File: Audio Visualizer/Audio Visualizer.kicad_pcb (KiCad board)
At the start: 2 copper layers, 103.5 x 30.2 mm, 120 parts, among them J1 Screw_Terminal_01x04, J2 Screw_Terminal_01x04, J3 Screw_Terminal_01x02, Q10 MMBT3904, Q11 MMBT3904, Q12 MMBT3904, Q13 MMBT3904, Q14 MMBT3904, Q15 MMBT3904, Q16 MMBT3904, Q17 MMBT3904, Q18 MMBT3904, Q19 MMBT3904, Q2 MMBT3904, Q20 MMBT3904, Q21 MMBT3904, Q3 MMBT3904, Q4 MMBT3904, Q5 MMBT3904, Q6 MMBT3904, Q7 MMBT3904, Q8 MMBT3904, Q9 MMBT3904, U1 LM358

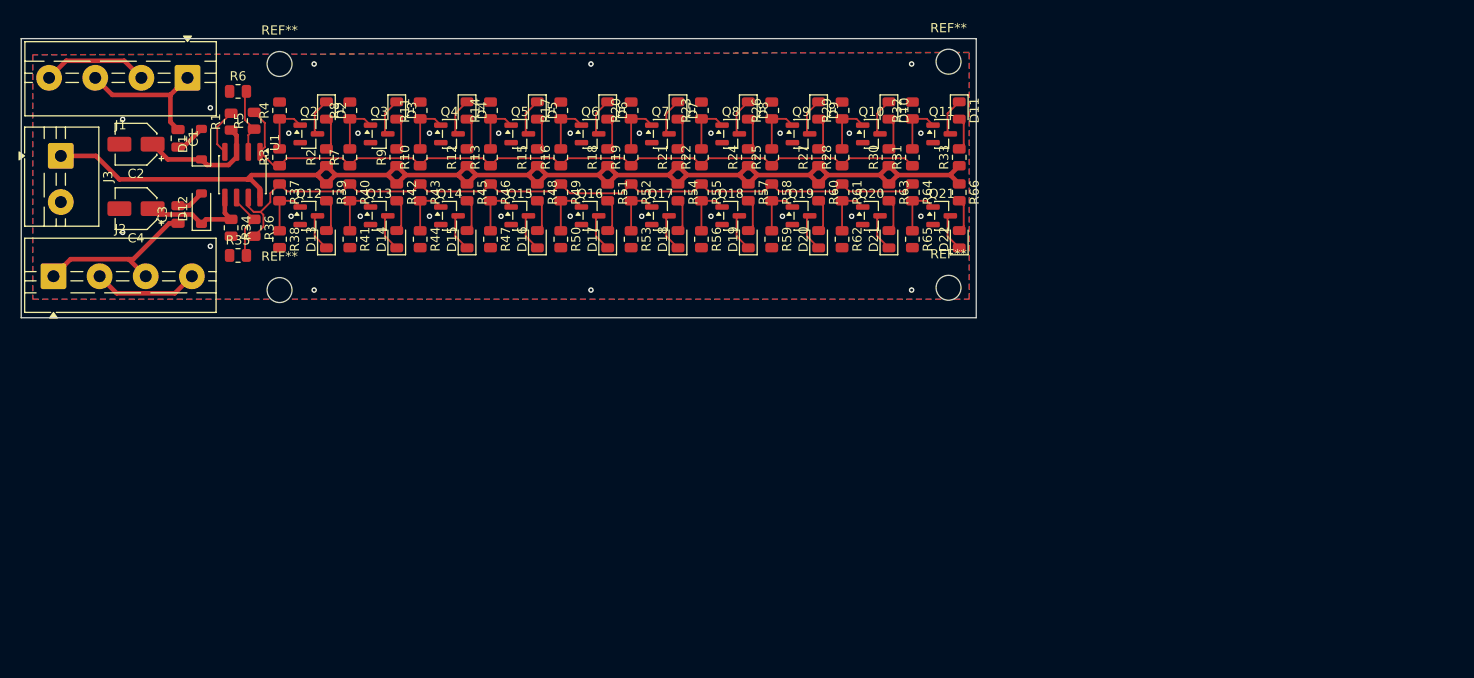
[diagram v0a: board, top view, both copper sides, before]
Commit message: Audio Visualizer: move terminal blocks and electrolytics to back side
Front face now flush for the LED ladder. THT terminals flipped with pads
kept on the same holes/nets; SMD electrolytics reconnected to front
traces with a via per pad; GND zones refilled. DRC: 0 errors,
0 unconnected. Adds back-side render.

Co-Authored-By: Claude Fable 5 <noreply@anthropic.com>
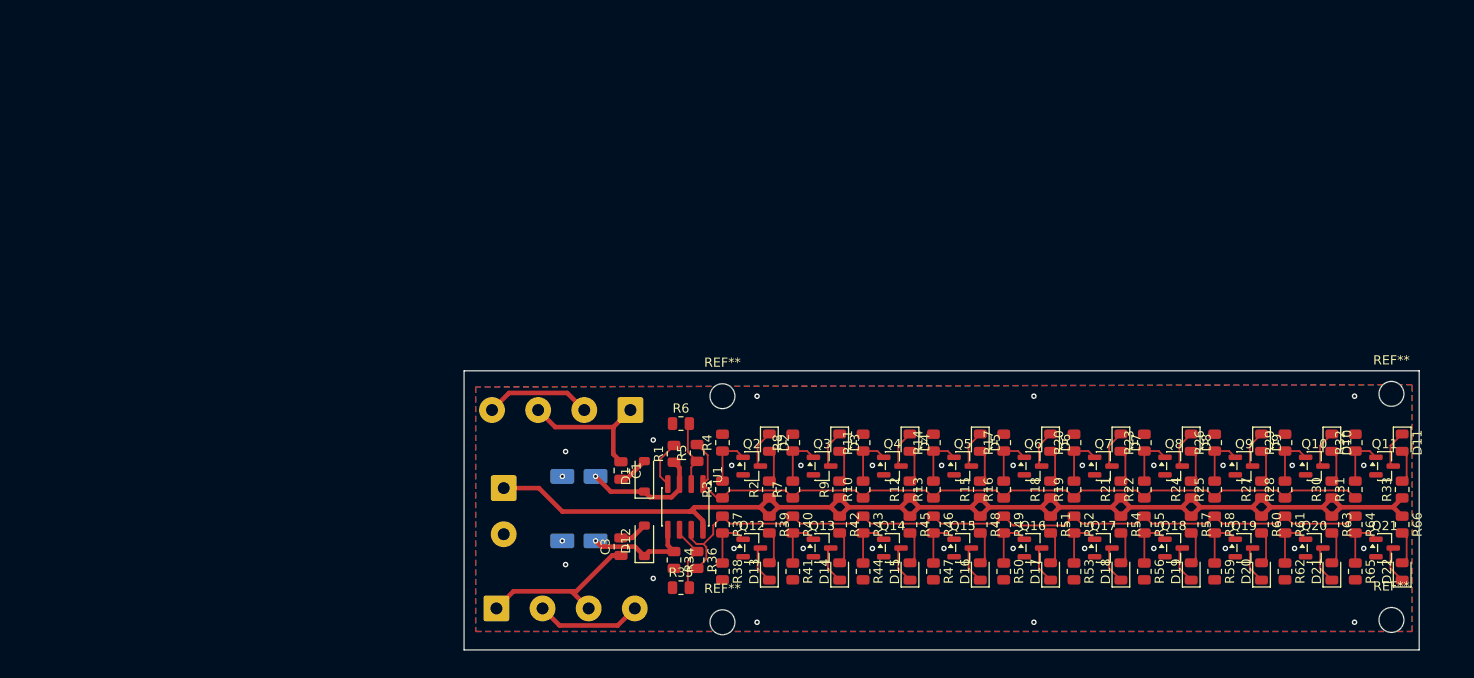
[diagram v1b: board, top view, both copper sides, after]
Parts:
- C2, C4, J1, J2, J3: moved to B.Cu
- moved C1 60.0 mm to (103.2, 95.1)
- moved C3 60.0 mm to (103.2, 103.3)
- moved D19 60.0 mm to (165.1, 106.0)
- moved D8 60.0 mm to (165.1, 92.0)
- moved J1 60.0 mm to (104.3, 88.5)
- moved Q18 60.0 mm to (163.1, 103.5)
- moved Q8 60.0 mm to (163.1, 94.6)
- moved R10 60.0 mm to (129.5, 97.1)
- moved R11 60.0 mm to (129.5, 92.0)
- moved R13 60.0 mm to (137.1, 97.1)
- moved R14 60.0 mm to (137.1, 92.0)
- moved R24 60.0 mm to (165.1, 97.1)
- moved R28 60.0 mm to (175.2, 97.1)
- moved R29 60.0 mm to (175.2, 92.0)
- moved R43 60.0 mm to (129.5, 100.9)
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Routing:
- net Net-(D1-K): vias 0 -> 1
- net Net-(D12-K): vias 0 -> 1
- net GND: vias 30 -> 32

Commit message: Audio Visualizer: face terminal block openings outward
Rotated J1/J2/J3 180deg about their pad rows (pin order reverses on the
holes) and swapped the matching net labels in the schematic (IN_L+/-,
IN_R+/-, +12V/GND) so every hole keeps its original net. Zones
refilled. DRC: 0 errors, 0 unconnected, 0 parity. All renders redone.

Co-Authored-By: Claude Fable 5 <noreply@anthropic.com>
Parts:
- moved J1 15.0 mm to (89.3, 88.5), turned to 0 degrees
- moved J2 15.0 mm to (104.8, 110.0), turned to 180 degrees
- moved J3 5.00 mm to (90.5, 102.0), turned to 90 degrees
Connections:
- J1 pad 1: /IN_R+ -> /IN_R-
- J1 pad 2: /IN_R- -> /IN_R+
- J1 pad 3: /IN_R+ -> /IN_R-
- J1 pad 4: /IN_R- -> /IN_R+
- J2 pad 1: /IN_L+ -> /IN_L-
- J2 pad 2: /IN_L- -> /IN_L+
- J2 pad 3: /IN_L+ -> /IN_L-
- J2 pad 4: /IN_L- -> /IN_L+
- J3 pad 1: /+12V -> GND
- J3 pad 2: GND -> /+12V

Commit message: Audio Visualizer: encode VU ladder LED colors (5 green, 4 orange, 1 red per row)
Co-Authored-By: Claude Fable 5 <noreply@anthropic.com>
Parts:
- D10, D18, D19, D20, D21, D7, D8, D9: value LED -> LED-ORANGE
- D11, D22: value LED -> LED-RED
- D13, D14, D15, D16, D17, D2, D3, D4, D5, D6: value LED -> LED-GREEN
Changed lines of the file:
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@@
 			)
 		)
-		(property "Value" "LED"
+		(property "Value" "LED-ORANGE"
 			(at 0 1.65 270)
 			(layer "F.Fab")
@@
 			)
 		)
-		(property "Value" "LED"
+		(property "Value" "LED-ORANGE"
 			(at 0 1.65 90)
 			(layer "F.Fab")
@@
 			)
 		)
-		(property "Value" "LED"
+		(property "Value" "LED-RED"
 			(at 0 1.65 90)
 			(layer "F.Fab")
@@
 			)
 		)
-		(property "Value" "LED"
+		(property "Value" "LED-GREEN"
 			(at 0 1.65 90)
 			(layer "F.Fab")
@@
 			)
 		)
-		(property "Value" "LED"
+		(property "Value" "LED-GREEN"
 			(at 0 1.65 270)
 			(layer "F.Fab")
@@
 			)
 		)
-		(property "Value" "LED"
+		(property "Value" "LED-ORANGE"
 			(at 0 1.65 270)
 			(layer "F.Fab")
@@
 			)
 		)
-		(property "Value" "LED"
+		(property "Value" "LED-ORANGE"
 			(at 0 1.65 90)
 			(layer "F.Fab")
@@
 			)
 		)
-		(property "Value" "LED"
+		(property "Value" "LED-ORANGE"
 			(at 0 1.65 90)
 			(layer "F.Fab")
@@
 			)
 		)
-		(property "Value" "LED"
+		(property "Value" "LED-GREEN"
 			(at 0 1.65 90)
 			(layer "F.Fab")
@@
 			)
 		)
-		(property "Value" "LED"
+		(property "Value" "LED-GREEN"
 			(at 0 1.65 270)
 			(layer "F.Fab")
@@
 			)
 		)
-		(property "Value" "LED"
+		(property "Value" "LED-ORANGE"
 			(at 0 1.65 90)
 			(layer "F.Fab")
@@
 			)
 		)
-		(property "Value" "LED"
+		(property "Value" "LED-ORANGE"
 			(at 0 1.65 270)
 			(layer "F.Fab")
@@
 			)
 		)
-		(property "Value" "LED"
+		(property "Value" "LED-GREEN"
 			(at 0 1.65 90)
 			(layer "F.Fab")
@@
 			)
 		)
-		(property "Value" "LED"
+		(property "Value" "LED-GREEN"
 			(at 0 1.65 270)
 			(layer "F.Fab")
@@
 			)
 		)
-		(property "Value" "LED"
+		(property "Value" "LED-ORANGE"
 			(at 0 1.65 270)
 			(layer "F.Fab")
@@
 			)
 		)
-		(property "Value" "LED"
+		(property "Value" "LED-GREEN"
 			(at 0 1.65 90)
 			(layer "F.Fab")
@@
 			)
 		)
-		(property "Value" "LED"
+		(property "Value" "LED-RED"
 			(at 0 1.65 270)
 			(layer "F.Fab")
@@
 			)
 		)
-		(property "Value" "LED"
+		(property "Value" "LED-GREEN"
 			(at 0 1.65 270)
 			(layer "F.Fab")
@@
 			)
 		)
-		(property "Value" "LED"
+		(property "Value" "LED-GREEN"
 			(at 0 1.65 270)
 			(layer "F.Fab")
@@
 			)
 		)
-		(property "Value" "LED"
+		(property "Value" "LED-GREEN"
 			(at 0 1.65 90)
 			(layer "F.Fab")

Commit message: Speaker Amp: JLC-stockable parts - 3225 crystal, XUNPU TS-1005B SMD side buttons
Y1 swapped to 2-pin-mapped 3225 footprint (basic-part crystals); SW1-SW3
swapped to SMD side-press switches (LCSC C2856783, machine-assembled),
rotated to face the board edge with bracket anchors at the edge. 3.3V
button rail moved to a B.Cu pad-via rail; HID1/HID2 rerouted on B.Cu
around the USB differential pair. DRC: 0 errors, 0 unconnected, 0 parity.

Co-Authored-By: Claude Fable 5 <noreply@anthropic.com>
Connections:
- J1 pad 1: /IN_R- -> /IN_R+
- J1 pad 2: /IN_R+ -> /IN_R-
- J1 pad 3: /IN_R- -> /IN_R+
- J1 pad 4: /IN_R+ -> /IN_R-
- J2 pad 1: /IN_L- -> /IN_L+
- J2 pad 2: /IN_L+ -> /IN_L-
- J2 pad 3: /IN_L- -> /IN_L+
- J2 pad 4: /IN_L+ -> /IN_L-
- J3 pad 2: /+12V -> GND
- R12 pad 1: /+12V -> GND
- R15 pad 1: /+12V -> GND
- R18 pad 1: /+12V -> GND
- R2 pad 1: /+12V -> GND
- R21 pad 1: /+12V -> GND
- R24 pad 1: /+12V -> GND
- R27 pad 1: /+12V -> GND
- R30 pad 1: /+12V -> GND
- R33 pad 1: /+12V -> GND
- R39 pad 1: /+12V -> GND
- R42 pad 1: /+12V -> GND
- R45 pad 1: /+12V -> GND
- R48 pad 1: /+12V -> GND
- R51 pad 1: /+12V -> GND
- R54 pad 1: /+12V -> GND
- R57 pad 1: /+12V -> GND
- R60 pad 1: /+12V -> GND
- R63 pad 1: /+12V -> GND
- R66 pad 1: /+12V -> GND
- R9 pad 1: /+12V -> GND
- U1 pad 8: /+12V -> GND
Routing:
- net GND: track 5.15 -> 141.5 mm
- net /+12V: track 136.3 -> 0.00 mm
- net /IN_L-: track 11.5 -> 0.00 mm
- net /IN_L+: track 18.5 -> 30.0 mm
- net /IN_R-: track 11.5 -> 0.00 mm
- net /IN_R+: track 15.6 -> 27.2 mm

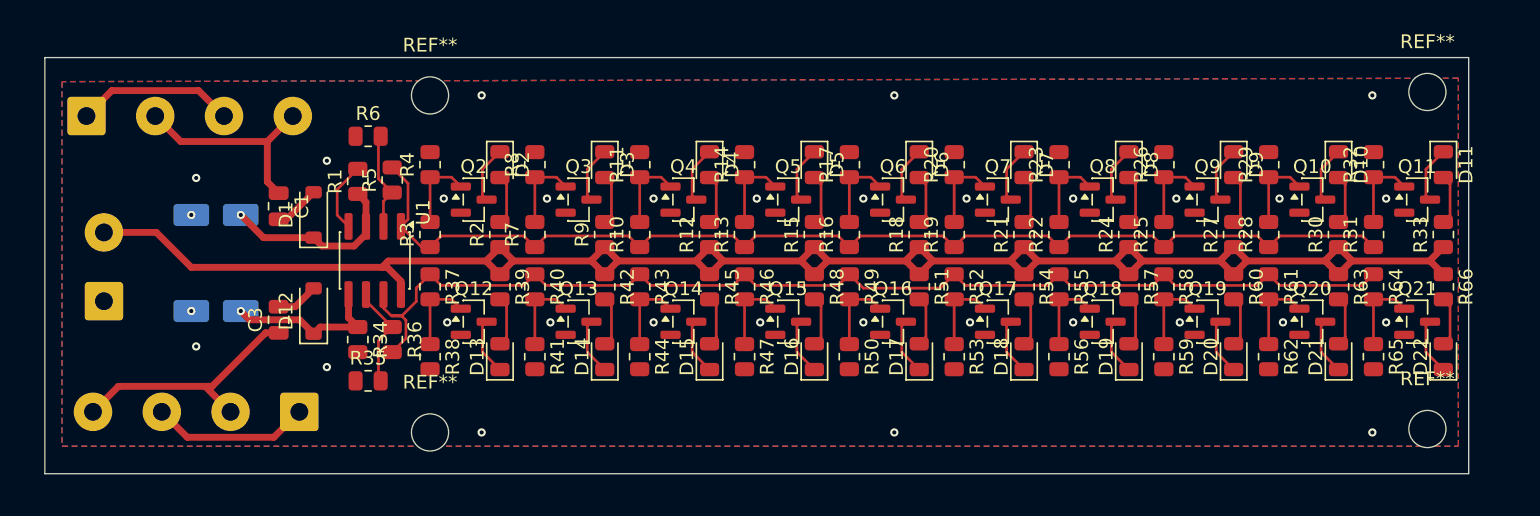
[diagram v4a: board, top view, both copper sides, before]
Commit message: Audio Visualizer: convert hand-solder parts to Detkin THT
- 20 ladder LEDs 0805 -> LED_THT:LED_D5.0mm (5mm, Detkin stock)
- C2/C4 10u electrolytics CP_Elec_4x5.4 -> CP_Radial_D5.0mm_P2.00mm (user's 100V BPSM2316)
- J1/J2 MX126 4P split into 2P pairs J4-J7 (user's schematic edit),
  all terminals incl. J3 now 4Ucon 1x02 3.5mm KF350-style (Detkin stock)
- zones refilled; DRC delta vs v1-smd: only stock-footprint courtyard/clearance
  notes from 5mm domes over SOT-23s, no new electrical violations

Co-Authored-By: Claude Fable 5 <noreply@anthropic.com>
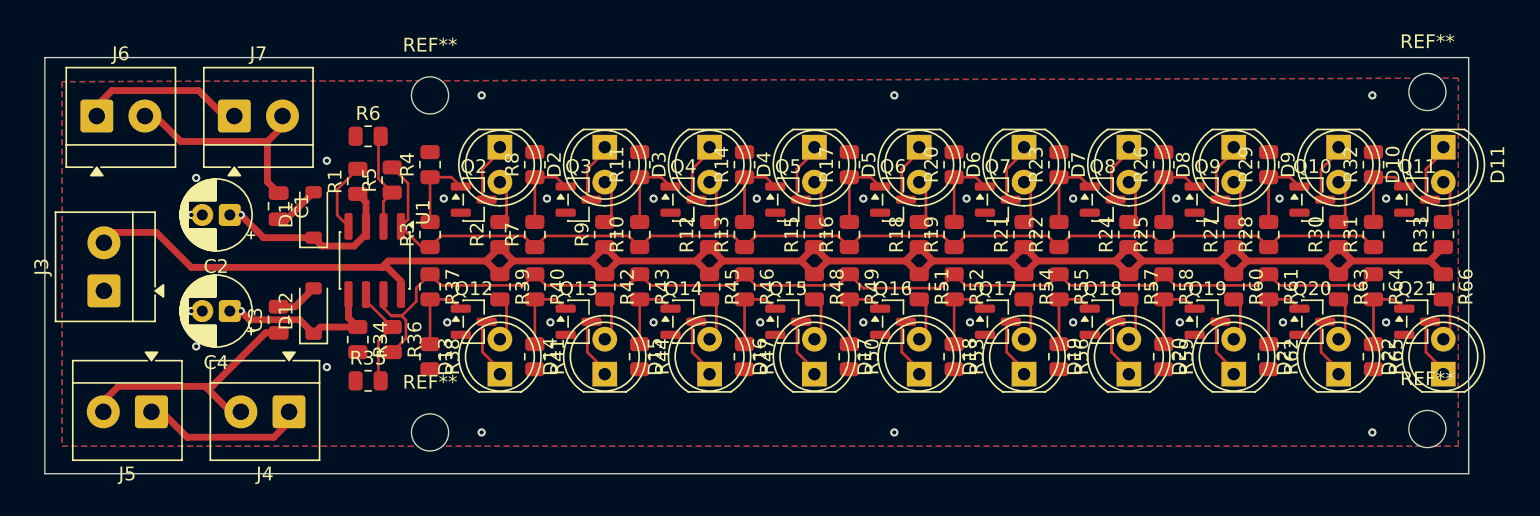
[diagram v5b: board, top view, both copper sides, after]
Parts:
- removed J1, J2: Screw_Terminal_01x04, TerminalBlock:TerminalBlock_MaiXu_MX126-5.0-04P_1x04_P5.00mm
- added J4: Screw_Terminal_01x02, TerminalBlock_4Ucon_1x02_P3.50mm_Horizontal, F.Cu at (104.0, 110.0)
- added J5: Screw_Terminal_01x02, TerminalBlock_4Ucon_1x02_P3.50mm_Horizontal, F.Cu at (94.0, 110.0)
- added J6: Screw_Terminal_01x02, TerminalBlock_4Ucon_1x02_P3.50mm_Horizontal, F.Cu at (90.0, 88.5)
- added J7: Screw_Terminal_01x02, TerminalBlock_4Ucon_1x02_P3.50mm_Horizontal, F.Cu at (100.0, 88.5)
- C2, C4: footprint Capacitor_SMD:CP_Elec_4x5.4 -> Capacitor_THT:CP_Radial_D5.0mm_P2.00mm; moved to F.Cu
- D10, D11, D13, D14, D15, D16, D17, D18, D19, D2, D20, D21, D22, D3, D4, D5, D6, D7, D8, D9: footprint LED_SMD:LED_0805_2012Metric -> LED_THT:LED_D5.0mm
- J3: footprint TerminalBlock:TerminalBlock_MaiXu_MX126-5.0-02P_1x02_P5.00mm -> TerminalBlock_4Ucon_1x02_P3.50mm_Horizontal; moved to F.Cu
- moved D10 1.27 mm to (180.3, 90.8)
- moved D11 1.27 mm to (187.9, 90.8)
- moved D13 1.27 mm to (119.3, 107.3)
- moved D14 1.27 mm to (127.0, 107.3)
- moved D15 1.27 mm to (134.6, 107.3)
- moved D16 1.27 mm to (142.2, 107.3)
- moved D17 1.27 mm to (149.8, 107.3)
- moved D18 1.27 mm to (157.4, 107.3)
- moved D19 1.27 mm to (165.1, 107.3)
- moved D2 1.27 mm to (119.3, 90.8)
- moved D20 1.27 mm to (172.7, 107.3)
- moved D21 1.27 mm to (180.3, 107.3)
- moved D22 1.27 mm to (187.9, 107.3)
- moved D3 1.27 mm to (127.0, 90.8)
- moved D4 1.27 mm to (134.6, 90.8)
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
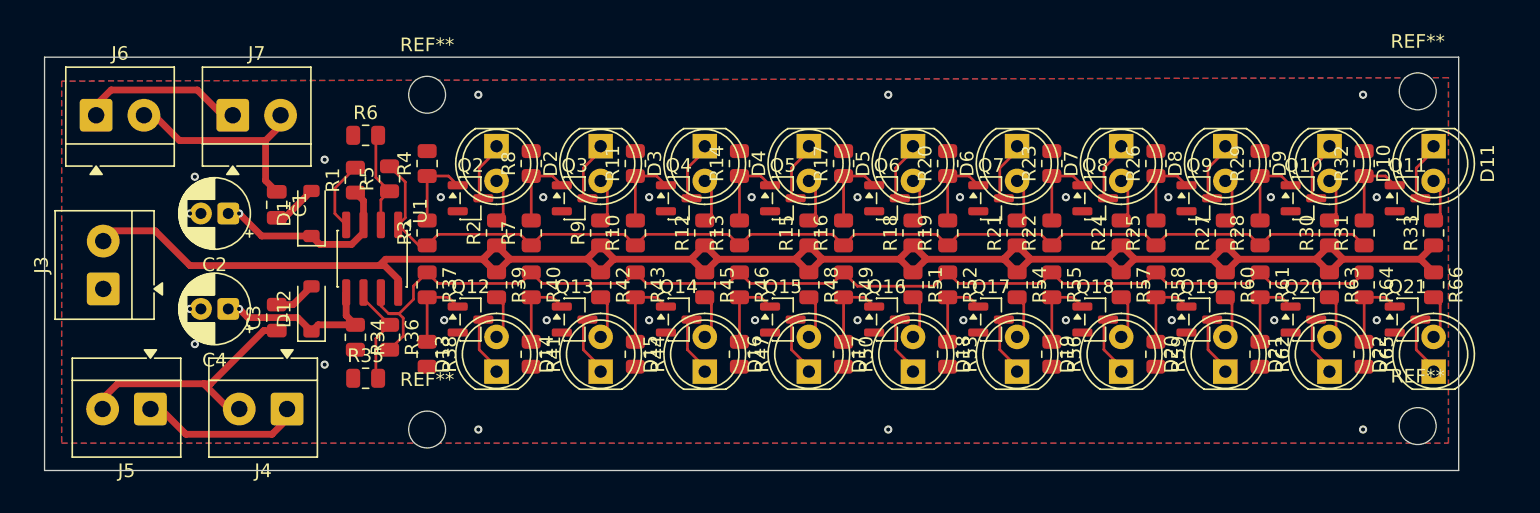
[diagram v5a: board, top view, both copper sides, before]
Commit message: Audio Visualizer V2: THT re-layout routed, 4K renders
- User re-layout: replicated cluster ladder at 6.985mm pitch, rails routed
- Two missing +12V stubs on template cluster (R2, R39) added; DRC now fully
  clean: 0 violations, 0 unconnected
- J3-J7 terminals use shipped Phoenix PT-1,5 3.5mm step model (4Ucon has none)
- V2 image set: Top / Top shadow / Corner / Back / PCB Layout

Co-Authored-By: Claude Fable 5 <noreply@anthropic.com>
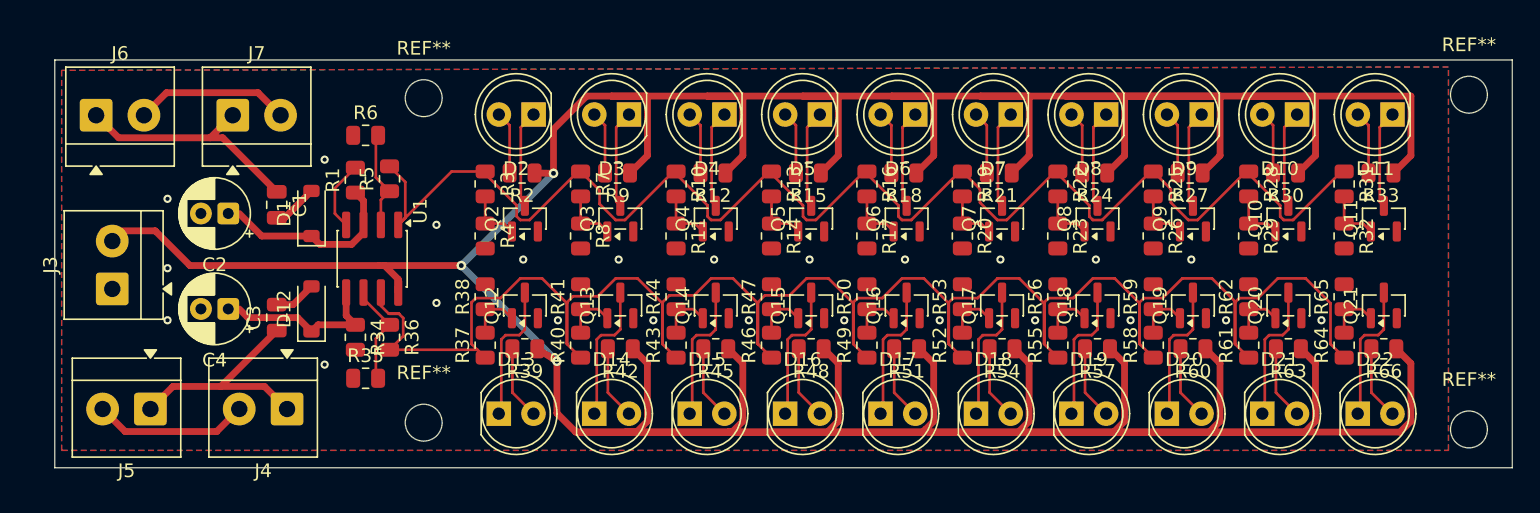
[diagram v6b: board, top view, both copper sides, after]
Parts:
- J3, J4, J5, J6, J7: footprint TerminalBlock_4Ucon_1x02_P3.50mm_Horizontal -> TerminalBlock_4Ucon:TerminalBlock_4Ucon_1x02_P3.50mm_Horizontal
- moved R4 6.80 mm to (118.5, 97.3), turned to -90 degrees
- moved R8 6.42 mm to (125.5, 97.3), turned to -90 degrees
- moved D22 6.35 mm to (182.4, 110.3), turned to 0 degrees
- moved R37 6.13 mm to (118.5, 105.3), turned to 90 degrees
- moved R11 6.08 mm to (132.5, 97.3), turned to -90 degrees
- moved R38 5.98 mm to (118.5, 101.8), turned to 90 degrees
- moved R66 5.93 mm to (184.3, 105.6), turned to 180 degrees
- moved R33 5.83 mm to (184.1, 92.7), turned to 180 degrees
- moved D21 5.80 mm to (175.4, 110.3), turned to 0 degrees
- moved R14 5.80 mm to (139.5, 97.3), turned to -90 degrees
- moved R40 5.71 mm to (125.5, 105.3), turned to 90 degrees
- moved R17 5.57 mm to (146.4, 97.3), turned to -90 degrees
- moved R3 5.56 mm to (118.5, 93.5), turned to -90 degrees
- moved R63 5.56 mm to (177.3, 105.6), turned to 180 degrees
- moved R41 5.55 mm to (125.5, 101.8), turned to 90 degrees
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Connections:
- J3 pad 2: GND -> /+12V
- R12 pad 1: GND -> /+12V
- R15 pad 1: GND -> /+12V
- R18 pad 1: GND -> /+12V
- R2 pad 1: GND -> /+12V
- R21 pad 1: GND -> /+12V
- R24 pad 1: GND -> /+12V
- R27 pad 1: GND -> /+12V
- R30 pad 1: GND -> /+12V
- R33 pad 1: GND -> /+12V
- R39 pad 1: GND -> /+12V
- R42 pad 1: GND -> /+12V
- R45 pad 1: GND -> /+12V
- R48 pad 1: GND -> /+12V
- R51 pad 1: GND -> /+12V
- R54 pad 1: GND -> /+12V
- R57 pad 1: GND -> /+12V
- R60 pad 1: GND -> /+12V
- R63 pad 1: GND -> /+12V
- R66 pad 1: GND -> /+12V
- R9 pad 1: GND -> /+12V
- U1 pad 8: GND -> /+12V
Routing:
- net /+12V: track 0.00 -> 388.7 mm, vias 0 -> 3
- net GND: track 141.5 -> 5.15 mm, vias 32 -> 24
- net /L_env: track 85.1 -> 158.3 mm
- net /R_env: track 82.7 -> 107.8 mm
- net /IN_L+: track 30.0 -> 17.2 mm
- net /IN_R-: track 0.00 -> 11.4 mm
- net /IN_L-: track 0.00 -> 11.4 mm
- net /IN_R+: track 27.2 -> 17.9 mm
- net Net-(D20-K): track 4.13 -> 10.2 mm
- net Net-(D16-K): track 4.13 -> 10.2 mm
- net Net-(D22-K): track 4.13 -> 10.2 mm
- net Net-(D15-K): track 4.13 -> 10.2 mm
- net Net-(D21-K): track 4.13 -> 10.2 mm
- net Net-(D18-K): track 4.13 -> 10.2 mm
- net Net-(D13-K): track 4.13 -> 10.2 mm
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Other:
- board size 103.5 x 30.2 mm -> 106.7 x 29.8 mm
